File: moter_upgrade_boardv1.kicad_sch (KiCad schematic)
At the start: 54 parts, among them J2 Conn_01x03_Socket, J3 Conn_01x02_Socket, J4 Conn_01x02_Socket, J5 Conn_01x02_Socket, J6 Conn_01x02_Socket, J7 Conn_ST_STDC14, J8 Conn_01x05_Socket, J9 USB_C_Receptacle_USB2.0_16P, SW1 SW_SPDT, SW2 SW_Push, SW3 SW_Wuerth_450301014042, U1 BD33FC0FP, U2 TLP785, U3 TLP785, U4 STM32H523CCTx, U5 MCP2562-E-P, U6 CH340E, U7 BD33FC0FP

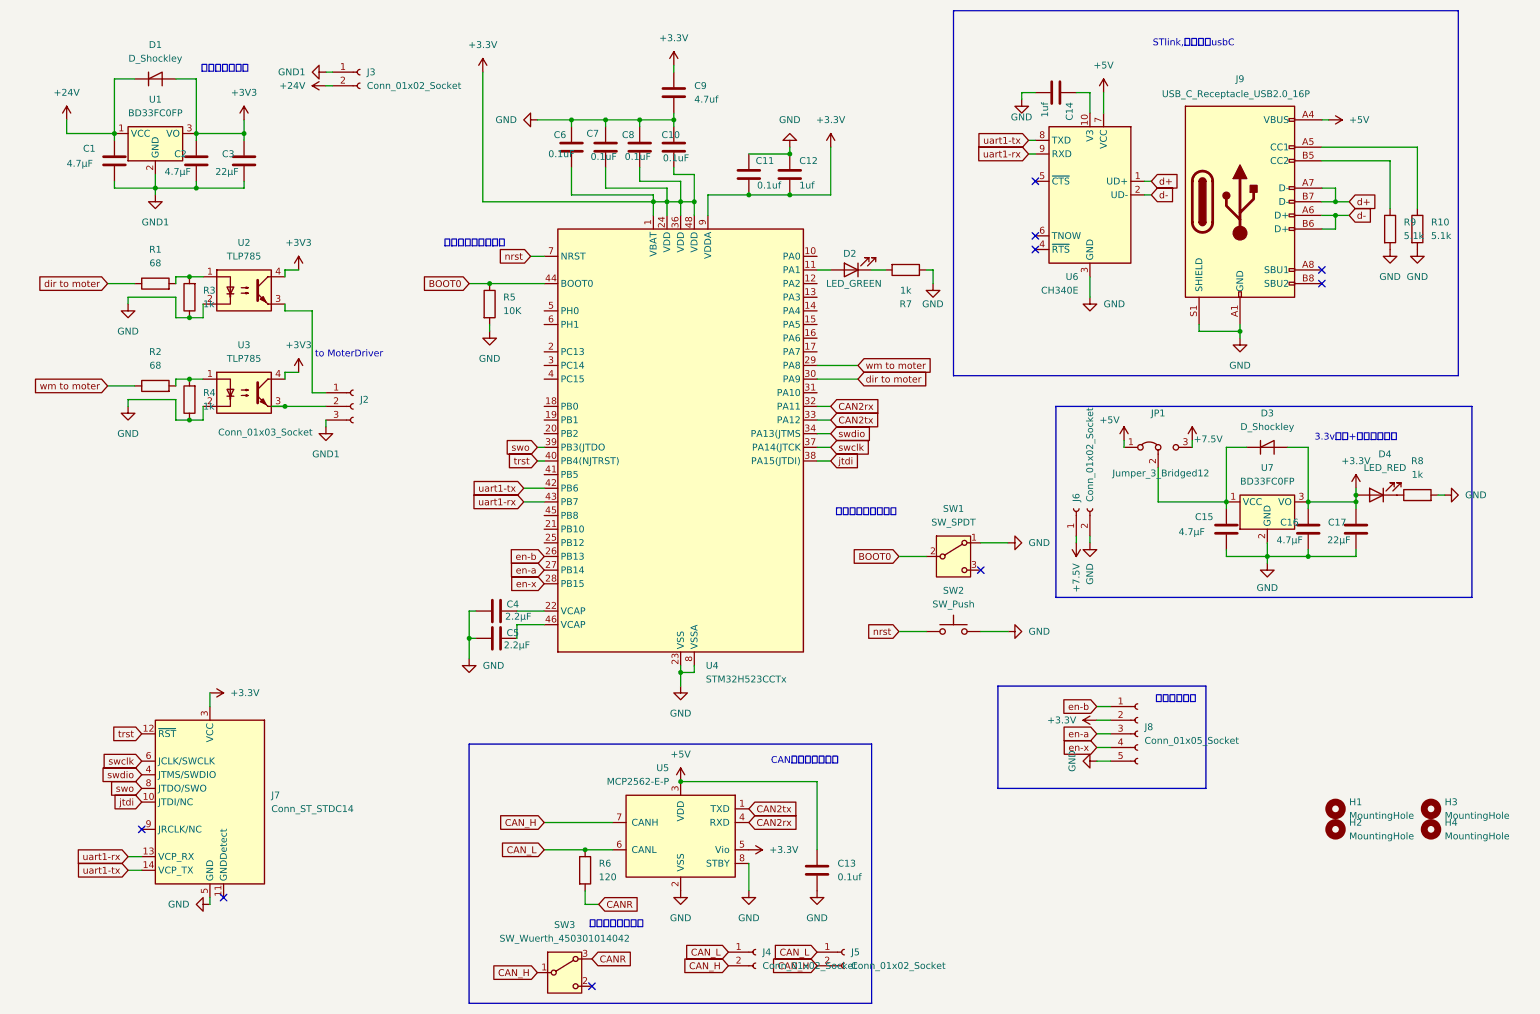
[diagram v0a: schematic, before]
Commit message: 基本構成の大幅変更(マイコンも変わった
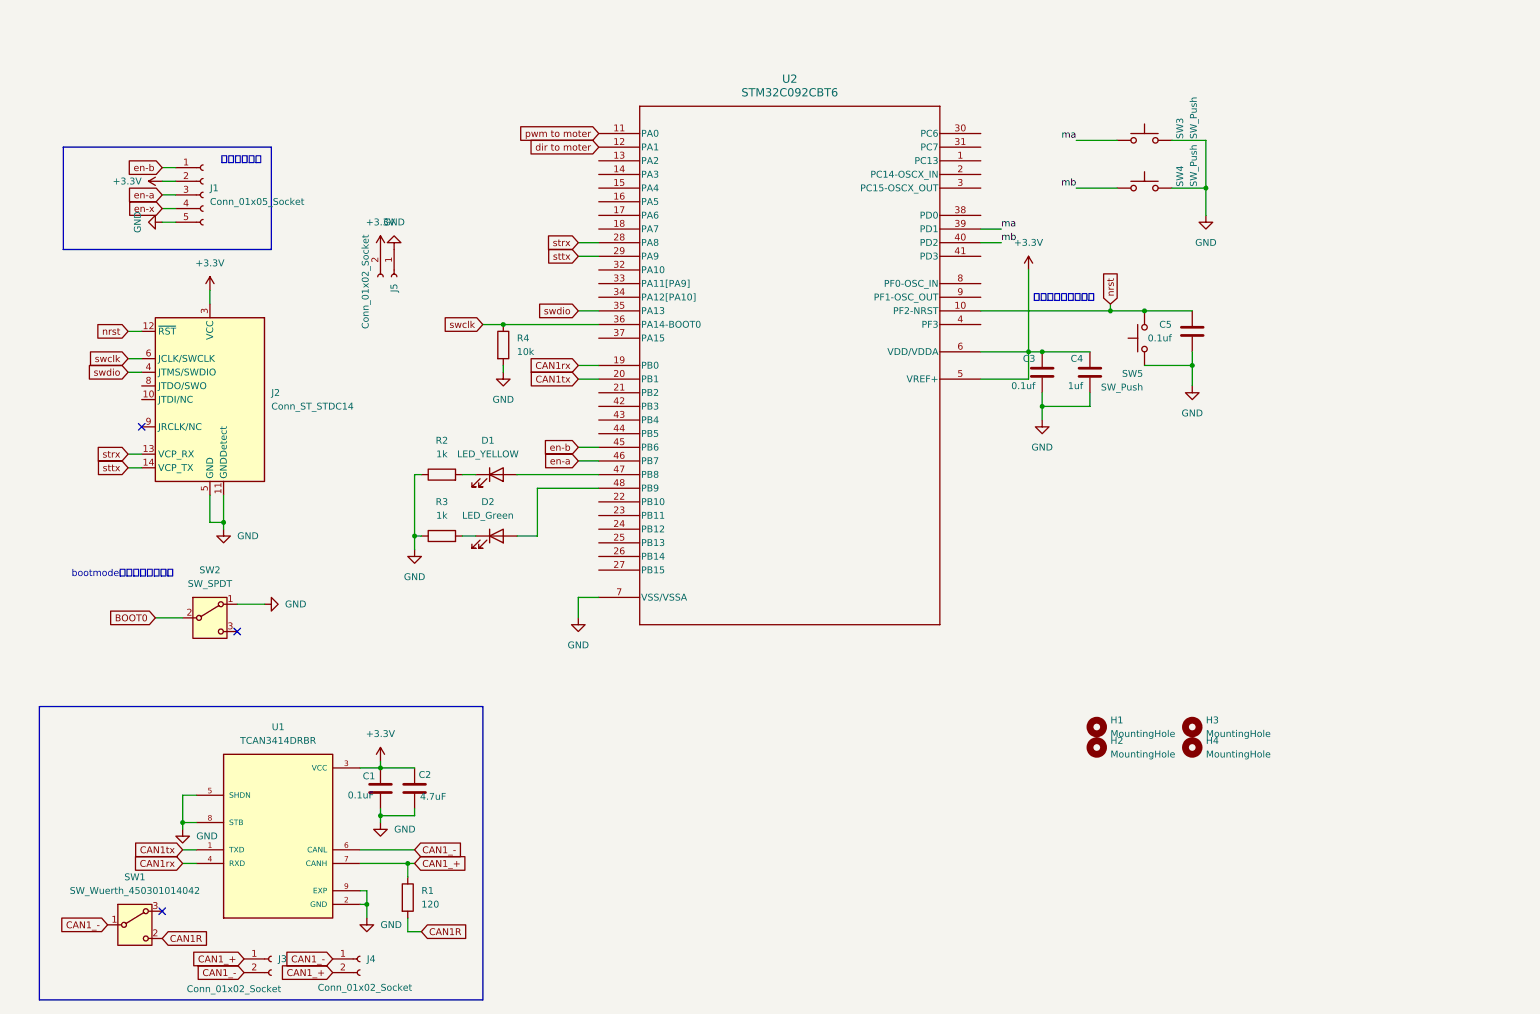
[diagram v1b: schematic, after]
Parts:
- removed C10, C6, C7, C8: 0.1uF, Capacitor_SMD:C_0603_1608Metric_Pad1.08x0.95mm_HandSolder, symbol Device:C
- removed C11, C13: 0.1uf, Capacitor_SMD:C_0603_1608Metric_Pad1.08x0.95mm_HandSolder, symbol Device:C
- removed C12, C14: 1uf, Capacitor_SMD:C_0603_1608Metric_Pad1.08x0.95mm_HandSolder, symbol Device:C
- removed C15, C16: 4.7μF, Capacitor_SMD:C_0805_2012Metric_Pad1.18x1.45mm_HandSolder, symbol Device:C
- removed C17: 22μF, Capacitor_SMD:C_0805_2012Metric_Pad1.18x1.45mm_HandSolder, symbol Device:C
- removed C9: 4.7uf, Capacitor_SMD:C_0805_2012Metric_Pad1.18x1.45mm_HandSolder, symbol Device:C
- removed D1, D3: D_Shockley, Diode_SMD:D_SOD-323_HandSoldering, symbol Device:D_Shockley
- removed D4: LED_RED, Capacitor_SMD:C_0603_1608Metric_Pad1.08x0.95mm_HandSolder, symbol Device:LED
- removed J2: Conn_01x03_Socket, Connector_PinHeader_2.54mm:PinHeader_1x03_P2.54mm_Vertical, symbol Connector:Conn_01x03_Socket
- removed J6: Conn_01x02_Socket, Connector_AMASS:AMASS_XT30PW-M_1x02_P2.50mm_Horizontal, symbol Connector:Conn_01x02_Socket
- removed J9: USB_C_Receptacle_USB2.0_16P, Connector_USB:USB_C_Receptacle_GCT_USB4105-xx-A_16P_TopMnt_Horizontal, symbol Connector:USB_C_Receptacle_USB2.0_16P
- removed JP1: Jumper_3_Bridged12, Connector_PinSocket_2.54mm:PinSocket_1x03_P2.54mm_Vertical, symbol Jumper:Jumper_3_Bridged12
- removed R10, R9: 5.1k, Resistor_SMD:R_0603_1608Metric_Pad0.98x0.95mm_HandSolder, symbol Device:R
- removed R5: 10K, Resistor_SMD:R_0603_1608Metric_Pad0.98x0.95mm_HandSolder, symbol Device:R
- removed R6: 120, Resistor_SMD:R_0603_1608Metric_Pad0.98x0.95mm_HandSolder, symbol Device:R
- removed R7, R8: 1k, Resistor_SMD:R_0603_1608Metric_Pad0.98x0.95mm_HandSolder, symbol Device:R
- removed SW2: SW_Push, Button_Switch_THT:SW_PUSH_6mm, symbol Switch:SW_Push
- removed SW3: SW_Wuerth_450301014042, Button_Switch_THT:SW_Slide-03_Wuerth-WS-SLTV_10x2.5x6.4_P2.54mm, symbol Switch:SW_Wuerth_450301014042
- removed U1, U7: BD33FC0FP, Package_TO_SOT_SMD:TO-252-2, symbol Regulator_Linear:BD33FC0FP
- removed U2, U3: TLP785, Package_DIP:DIP-4_W7.62mm, symbol Isolator:TLP785
- removed U4: STM32H523CCTx, Package_QFP:LQFP-48_7x7mm_P0.5mm, symbol MCU_ST_STM32H5:STM32H523CCTx
- removed U5: MCP2562-E-P, Package_DIP:DIP-8_W7.62mm, symbol Interface_CAN_LIN:MCP2562-E-P
- removed U6: CH340E, Package_SO:MSOP-10_3x3mm_P0.5mm, symbol Interface_USB:CH340E
- added D1: LED_YELLOW, Diode_SMD:D_0805_2012Metric_Pad1.15x1.40mm_HandSolder, symbol Device:LED
- added SW1: SW_Wuerth_450301014042, Button_Switch_THT:SW_Slide-03_Wuerth-WS-SLTV_10x2.5x6.4_P2.54mm, symbol Switch:SW_Wuerth_450301014042
- added SW3, SW4, SW5: SW_Push, Button_Switch_THT:SW_PUSH_6mm, symbol Switch:SW_Push
- added U1: TCAN3414DRBR, TCAN3414DRBR:XCVR_TCAN3414DRBR, symbol TCAN3414DRBR:TCAN3414DRBR
- added U2: STM32C092CBT6, stm32c092cbt6:LQFP48_STM, symbol stm32c092cbt6:STM32C092CBT6
- C1: value 4.7μF -> 0.1uF; footprint Capacitor_SMD:C_0805_2012Metric_Pad1.18x1.45mm_HandSolder -> Capacitor_SMD:C_0603_1608Metric_Pad1.08x0.95mm_HandSolder
- C2: value 4.7μF -> 4.7uF; footprint Capacitor_SMD:C_0805_2012Metric_Pad1.18x1.45mm_HandSolder -> Capacitor_SMD:C_0603_1608Metric_Pad1.08x0.95mm_HandSolder
- C3: value 22μF -> 0.1uf; footprint Capacitor_SMD:C_0805_2012Metric_Pad1.18x1.45mm_HandSolder -> Capacitor_SMD:C_0603_1608Metric_Pad1.08x0.95mm_HandSolder
- C4: value 2.2μF -> 1uf
- C5: value 2.2μF -> 0.1uf
- D2: value LED_GREEN -> LED_Green; footprint Capacitor_SMD:C_0603_1608Metric_Pad1.08x0.95mm_HandSolder -> Diode_SMD:D_0805_2012Metric_Pad1.15x1.40mm_HandSolder
- J3: footprint Connector_AMASS:AMASS_XT30PW-M_1x02_P2.50mm_Horizontal -> Connector_JST:JST_XH_S2B-XH-A-1_1x02_P2.50mm_Horizontal
- R1: value 68 -> 120
- R2: value 68 -> 1k
- R4: value 1k -> 10k
- renumbered J8 to J1, J7 to J2, SW1 to SW2
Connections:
- net trst is gone; now on net nrst: J2.12 (~{RST})
- net wm to moter is gone; now on net GND: R2.1
- net +3.3V: now also C1.2, C2.2, C3.1, C4.1, J5.2 (Pin_2), U1.3 (VCC), U2.5 (VREF+), U2.6 (VDD/VDDA)
- net GND: now also C1.1, C2.1, C3.2, C4.2, C5.2, J2.11 (GNDDetect), J5.1 (Pin_1), R4.2, SW3.2, SW4.2, SW5.2, U1.2 (GND), U1.5 (SHDN), U1.8 (STB), U1.9 (EXP), U2.7 (VSS/VSSA); no longer C4.1, C5.1, R4.1
- net dir to moter: now also U2.12 (PA1); no longer R1.1
- net en-a: now also U2.46 (PB7)
- net en-b: now also U2.45 (PB6)
- net nrst: now also C5.1, SW5.1, U2.10 (PF2-NRST)
- net swclk: now also R4.1, U2.36 (PA14-BOOT0)
- net swdio: now also U2.35 (PA13)
- net at R2.2: now also D1.1 (K); no longer R4.2
- net at R3.2: now also D2.1 (K); no longer R1.2
- net at D2.2 (A): now also U2.48 (PB9)
- net +24V renamed CAN1_-
- net CAN1_-: now also J4.1 (Pin_1), SW1.1 (B), U1.6 (CANL); no longer C1.1
- removed net +3V3: C2.1, C3.1
- net CAN_H renamed CAN1_+
- net CAN1_+: now also J3.1 (Pin_1), R1.1, U1.7 (CANH); no longer J5.2 (Pin_2)
- removed net CAN_L: J4.1 (Pin_1), J5.1 (Pin_1)
- removed net GND1: C1.2, C2.2, C3.2, J3.1 (Pin_1)
- net jtdi: no longer names the net of J2.10 (JTDI/NC)
- net swo: no longer names the net of J2.8 (JTDO/SWO)
- net uart1-rx renamed strx
- net strx: now also U2.28 (PA8)
- net uart1-tx renamed sttx
- net sttx: now also U2.29 (PA9)
- new net: D1.2 (A), U2.47 (PB8)
- new net CAN1R: R1.2, SW1.2 (C)
- new net CAN1rx: U1.4 (RXD), U2.19 (PB0)
- new net CAN1tx: U1.1 (TXD), U2.20 (PB1)
- new net ma: SW3.1, U2.39 (PD1)
- new net mb: SW4.1, U2.40 (PD2)
- new net pwm to moter: U2.11 (PA0)
- no-connect marks 9 -> 3
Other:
- note added: "bootmode切り替えスイッチ"
- note removed: "3.3v変圧+逆流防止回路"
- note removed: "CANトランシーバー"
- note removed: "STlink,電源供給usbC"
- note removed: "to MoterDriver"
- note removed: "終端抵抗オンオフ"
- note removed: "絶縁信号の電源"
- moved on the sheet: H1, H2, H3, H4, J1, J2, SW2

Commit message: ver2完成発注(データ同梱)
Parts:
- removed SW2: SW_SPDT, Button_Switch_THT:SW_Slide-03_Wuerth-WS-SLTV_10x2.5x6.4_P2.54mm, symbol Switch:SW_SPDT
- added J6: Conn_01x03_Pin, TerminalBlock_RND:TerminalBlock_RND_205-00233_1x03_P5.08mm_Horizontal, symbol Connector:Conn_01x03_Pin
- added R5, R6, R7, R8: 10k, Resistor_SMD:R_0805_2012Metric, symbol Device:R
- R4: footprint Resistor_SMD:R_0603_1608Metric_Pad0.98x0.95mm_HandSolder -> Resistor_SMD:R_0805_2012Metric
- renumbered SW3 to SW2, SW4 to SW3, SW5 to SW4
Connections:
- net +3.3V: now also R5.1, R6.1, R7.1, R8.1
- net GND: now also J6.3 (Pin_3)
- net dir to moter: now also J6.1 (Pin_1)
- net ma: now also U2.26 (PB14), R7.2; no longer U2.39 (PD1)
- net mb: now also U2.25 (PB13), R5.2; no longer U2.40 (PD2)
- net nrst: now also R6.2
- net pwm to moter: now also J6.2 (Pin_2)
- net swdio: now also R8.2
- net at D1.2 (A): now also U2.24 (PB12); no longer U2.47 (PB8)
- net at D2.2 (A): now also U2.23 (PB11); no longer U2.48 (PB9)
- no-connect marks 3 -> 2
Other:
- note removed: "bootmode切り替えスイッチ"
